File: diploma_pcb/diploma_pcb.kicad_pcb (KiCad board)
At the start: 2 copper layers, 50 x 24 mm, 16 parts, among them Q1 2SC3356, Q3 2SC3356

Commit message: with capacitors
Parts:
- added C1: .1uF, Capacitor_SMD:C_1206_3216Metric_Pad1.33x1.80mm_HandSolder, F.Cu at (36.3, 57.3)
- added C2: .1uF, Capacitor_SMD:C_1206_3216Metric_Pad1.33x1.80mm_HandSolder, F.Cu at (55.3, 60.0)
- added C3: .1uF, Capacitor_SMD:C_1206_3216Metric_Pad1.33x1.80mm_HandSolder, F.Cu at (38.5, 67.2)
- moved R6 6.67 mm to (46.8, 59.8)
- moved R_gnd1 5.57 mm to (63.8, 61.7)
- moved R3 3.87 mm to (54.2, 57.2), turned to 0 degrees
- moved R2 3.75 mm to (41.6, 62.2), turned to 180 degrees
- moved R5 3.32 mm to (60.2, 60.6)
- moved Q1 3.20 mm to (35.7, 61.4), turned to -90 degrees
- moved RData1 3.18 mm to (41.6, 64.5)
- moved 8_pin_op_amp1 2.77 mm to (54.8, 64.9), turned to 90 degrees
- moved R4 2.63 mm to (59.0, 57.2)
- moved Q3 2.19 mm to (30.6, 61.9)
- moved R1 1.77 mm to (41.6, 59.9)
- moved C104 1.72 mm to (33.9, 64.9)
- moved Rcc1 1.65 mm to (63.9, 59.4)
- moved R7 1.57 mm to (64.0, 57.1)
- moved 5_pins_op_amp1 1.26 mm to (47.1, 66.0), turned to 180 degrees
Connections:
- 8_pin_op_amp1 pad 7: Net-(5_pins_op_amp1-VDD) -> Net-(8_pin_op_amp1-V+)
- R1 pad 2: Net-(5_pins_op_amp1-VDD) -> Net-(C1-Pad2)
- R6 pad 1: Net-(5_pins_op_amp1-VDD) -> Net-(C1-Pad2)
- R7 pad 1: Net-(5_pins_op_amp1-VDD) -> Net-(C1-Pad2)
- Rcc1 pad 1: Net-(5_pins_op_amp1-VDD) -> Net-(C1-Pad2)
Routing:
- net Net-(5_pins_op_amp1-VSS): track 56.1 -> 0.00 mm
- net Net-(5_pins_op_amp1-VDD): track 55.8 -> 0.00 mm
- net Net-(5_pins_op_amp1-VOUT): track 44.6 -> 0.00 mm
- net Net-(5_pins_op_amp1-VIN+): track 23.9 -> 0.00 mm
- net Net-(5_pins_op_amp1-VIN-): track 19.6 -> 0.00 mm
- net Net-(A1-A0): track 17.6 -> 0.00 mm
- net Net-(Q1-C): track 10.7 -> 0.00 mm
- net Net-(A1-3V3): track 4.20 -> 0.00 mm
- net Net-(Q1-B): track 3.40 -> 0.00 mm
- net Net-(A1-+5V): track 3.35 -> 0.00 mm
- net Net-(C104-Pad2): track 2.89 -> 0.00 mm

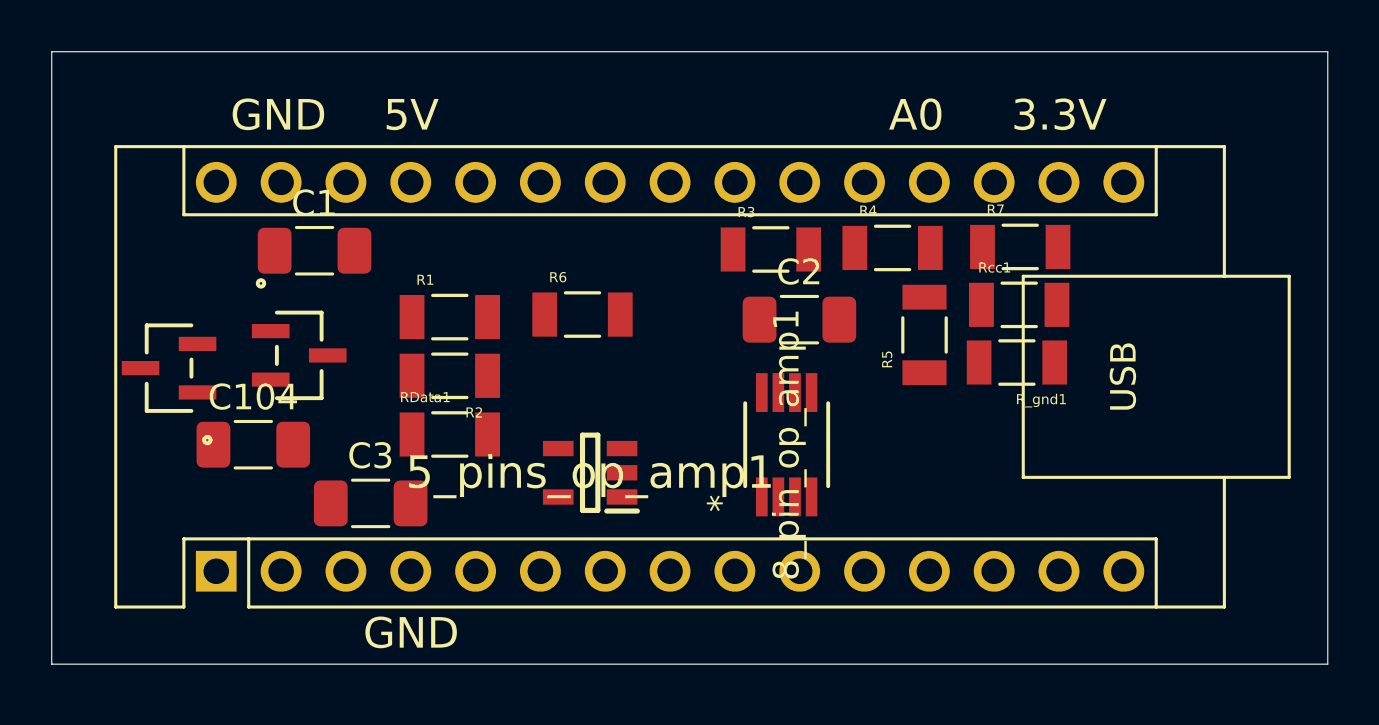
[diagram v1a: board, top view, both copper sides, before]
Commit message: Fixed schematic with dimplomer
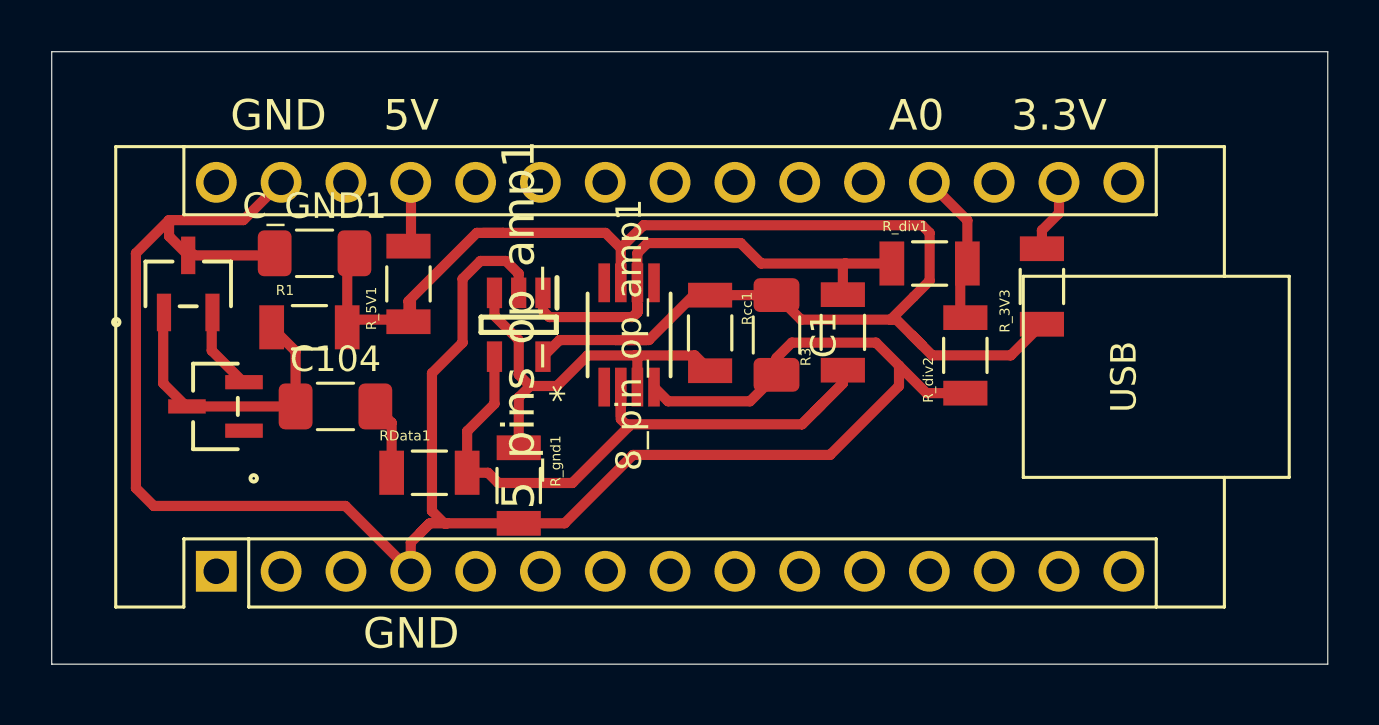
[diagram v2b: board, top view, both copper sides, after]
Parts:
- removed C2, C3: .1uF, Capacitor_SMD:C_1206_3216Metric_Pad1.33x1.80mm_HandSolder
- removed R2: R, 1206:RESC3116X65N
- added C1: .1uF, Capacitor_SMD:C_1206_3216Metric_Pad1.33x1.80mm_HandSolder, F.Cu at (54.4, 60.6)
- moved R_gnd1 20.1 mm to (44.3, 66.5), turned to -90 degrees
- moved Rcc1 12.2 mm to (51.8, 60.5), turned to -90 degrees
- moved 8_pin_op_amp1 7.52 mm to (48.6, 60.6)
- moved R_5V1 6.92 mm to (40.0, 58.6), turned to 90 degrees
- moved 5_pins_op_amp1 6.44 mm to (44.3, 60.2), turned to -90 degrees
- moved R1 5.51 mm to (36.1, 60.3)
- moved R3 4.30 mm to (57.0, 60.5), turned to 90 degrees
- moved Q1 3.84 mm to (32.4, 63.4), turned to 90 degrees
- moved C104 3.55 mm to (37.1, 63.4)
- moved Q3 3.38 mm to (31.3, 58.6), turned to 0 degrees
- moved R_div2 1.79 mm to (61.8, 61.4)
- moved R_3V3 1.77 mm to (64.8, 58.7), turned to 90 degrees
- moved RData1 1.70 mm to (40.8, 66.0)
- moved R_div1 1.57 mm to (60.4, 57.8)
- moved C_GND1 0.10 mm to (36.3, 57.4)
- renumbered C1 to C_GND1, R7 to R_3V3, R6 to R_5V1, R4 to R_div1, R5 to R_div2
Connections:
- net Net-(5_pins_op_amp1-VIN-) renamed signal
- net Net-(5_pins_op_amp1-VSS) renamed GND
- 5_pins_op_amp1 pad 5: Net-(5_pins_op_amp1-VDD) -> Supply
- 8_pin_op_amp1 pad 7: Net-(8_pin_op_amp1-V+) -> Supply
- C_GND1 pad 2: Net-(C1-Pad2) -> Supply
- R1 pad 2: Net-(C1-Pad2) -> Supply
- R_3V3 pad 1: Net-(C1-Pad2) -> Supply
- R_5V1 pad 1: Net-(C1-Pad2) -> Supply
- Rcc1 pad 1: Net-(C1-Pad2) -> Supply
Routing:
- net GND: track 0.00 -> 86.1 mm
- net Supply: track 0.00 -> 60.6 mm
- net signal: track 0.00 -> 27.5 mm
- net Net-(5_pins_op_amp1-VOUT): track 0.00 -> 19.1 mm
- net Net-(5_pins_op_amp1-VIN+): track 0.00 -> 15.9 mm
- net Net-(Q1-C): track 0.00 -> 11.7 mm
- net Net-(A1-A0): track 0.00 -> 6.03 mm
- net Net-(Q1-B): track 0.00 -> 3.04 mm
- net Net-(A1-3V3): track 0.00 -> 2.88 mm
- net Net-(C104-Pad2): track 0.00 -> 2.86 mm
- net Net-(A1-+5V): track 0.00 -> 1.67 mm

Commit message: rgb placed
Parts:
- added LED1: MP008253, MP008253:MP008253, F.Cu at (69.5, 60.0)
- added R_LED_B1: R, Resistor_SMD:R_1206_3216Metric, F.Cu at (60.5, 65.0)
- added R_LED_G1: R, Resistor_SMD:R_1206_3216Metric, F.Cu at (60.5, 67.5)
- added R_LED_R1: R, Resistor_SMD:R_1206_3216Metric, F.Cu at (65.5, 67.5)
- R1, R3, RData1, R_3V3, R_5V1, R_div1, R_div2, R_gnd1, Rcc1: footprint 1206:RESC3116X65N -> Resistor_SMD:R_1206_3216Metric
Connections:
- A1 pad 11: unconnected-(A1-D8-Pad11) -> Net-(A1-D8)
- A1 pad 12: unconnected-(A1-D9-Pad12) -> Net-(A1-D9)
- A1 pad 13: unconnected-(A1-D10-Pad13) -> Net-(A1-D10)
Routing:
- net Net-(LED1-A_GREEN): track 0.00 -> 0.71 mm
- net Net-(LED1-A_RED): track 0.00 -> 0.57 mm

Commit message: Working Serial Comunication!
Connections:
- net Net-(5_pins_op_amp1-VIN+) renamed non inv
- net Net-(5_pins_op_amp1-VOUT) renamed Vout
- net Net-(A1-+5V) renamed 5V
- net Net-(A1-3V3) renamed 3.3V
- net Net-(LED1-A_BLUE) renamed blue
- net Net-(LED1-A_GREEN) renamed green
- net Net-(LED1-A_RED) renamed red
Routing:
- net green: track 0.71 -> 11.0 mm
- net GND: track 86.1 -> 96.1 mm
- net blue: track 0.00 -> 6.99 mm
- net red: track 0.57 -> 7.33 mm
- net Net-(A1-D8): track 0.00 -> 5.35 mm
- net Net-(A1-D9): track 0.00 -> 2.92 mm
- net Net-(A1-D10): track 0.00 -> 2.82 mm
